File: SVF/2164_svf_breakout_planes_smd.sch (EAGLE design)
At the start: 87 parts, among them IC1 SSM2164S, IC2 TL072, IC3 TL072, IC4 TL072, IC5 TL072, IC6 TL072, U1 THONKICONNNEW, U2 THONKICONNNEW, U3 THONKICONNNEW, U4 THONKICONNNEW, U5 THONKICONNNEW, U6 THONKICONNNEW

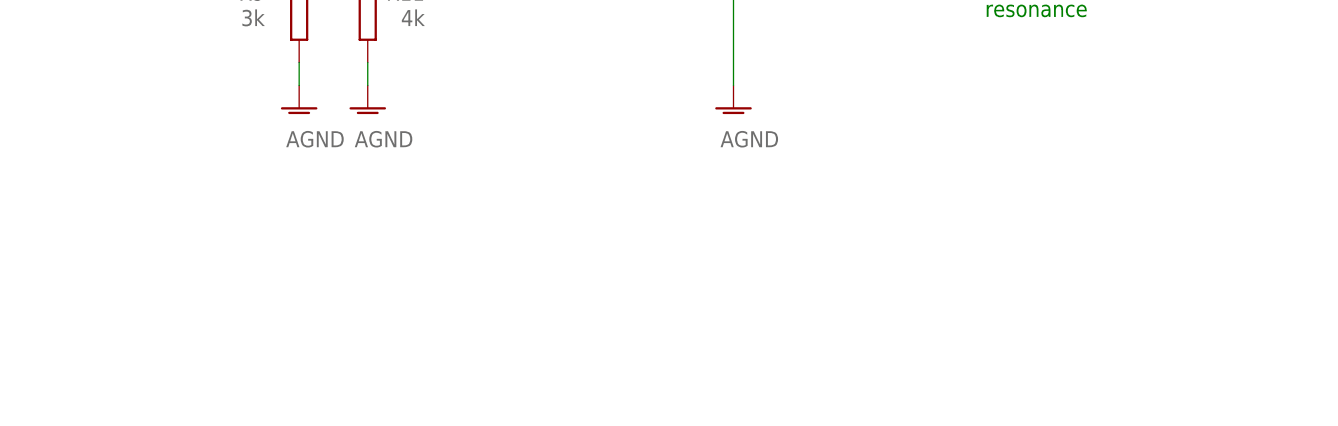
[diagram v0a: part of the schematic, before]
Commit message: Add SMD 0603 version of SVF
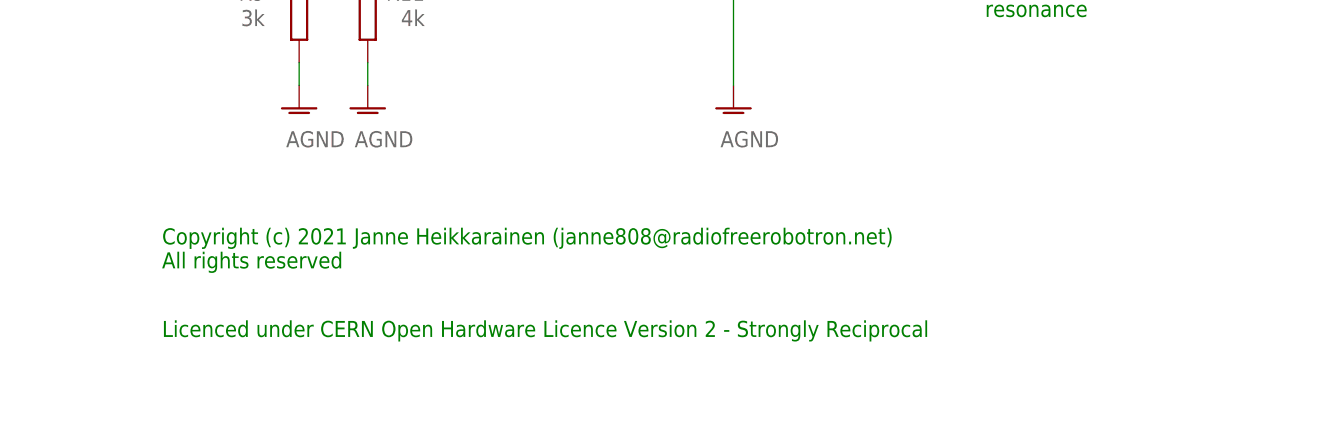
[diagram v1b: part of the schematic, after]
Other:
- note added: "Copyright (c) 2021 Janne Heikkarainen (janne808@radiofreerobotron.net) All rights reserved"
- note added: "Licenced under CERN Open Hardware Licence Version 2 - Strongly Reciprocal"
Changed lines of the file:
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@@
 <grid distance="0.1" unitdist="inch" unit="inch" style="lines" multiple="1" display="no" altdistance="0.01" altunitdist="inch" altunit="inch"/>
 <layers>
-<layer number="1" name="Top" color="4" fill="1" visible="yes" active="no"/>
-<layer number="2" name="Route2" color="16" fill="1" visible="yes" active="no"/>
-<layer number="3" name="Route3" color="17" fill="1" visible="yes" active="no"/>
-<layer number="4" name="Route4" color="18" fill="1" visible="yes" active="no"/>
-<layer number="5" name="Route5" color="19" fill="1" visible="yes" active="no"/>
-<layer number="6" name="Route6" color="25" fill="1" visible="yes" active="no"/>
-<layer number="7" name="Route7" color="26" fill="1" visible="yes" active="no"/>
-<layer number="8" name="Route8" color="27" fill="1" visible="yes" active="no"/>
-<layer number="9" name="Route9" color="28" fill="1" visible="yes" active="no"/>
-<layer number="10" name="Route10" color="29" fill="1" visible="yes" active="no"/>
-<layer number="11" name="Route11" color="30" fill="1" visible="yes" active="no"/>
-<layer number="12" name="Route12" color="20" fill="1" visible="yes" active="no"/>
-<layer number="13" name="Route13" color="21" fill="1" visible="yes" active="no"/>
-<layer number="14" name="Route14" color="22" fill="1" visible="yes" active="no"/>
-<layer number="15" name="Route15" color="23" fill="1" visible="yes" active="no"/>
-<layer number="16" name="Bottom" color="1" fill="1" visible="yes" active="no"/>
-<layer number="17" name="Pads" color="2" fill="1" visible="yes" active="no"/>
-<layer number="18" name="Vias" color="2" fill="1" visible="yes" active="no"/>
-<layer number="19" name="Unrouted" color="6" fill="1" visible="yes" active="no"/>
-<layer number="20" name="Dimension" color="24" fill="1" visible="yes" active="no"/>
-<layer number="21" name="tPlace" color="7" fill="1" visible="yes" active="no"/>
-<layer number="22" name="bPlace" color="7" fill="1" visible="yes" active="no"/>
-<layer number="23" name="tOrigins" color="15" fill="1" visible="yes" active="no"/>
-<layer number="24" name="bOrigins" color="15" fill="1" visible="yes" active="no"/>
-<layer number="25" name="tNames" color="7" fill="1" visible="yes" active="no"/>
-<layer number="26" name="bNames" color="7" fill="1" visible="yes" active="no"/>
-<layer number="27" name="tValues" color="7" fill="1" visible="yes" active="no"/>
-<layer number="28" name="bValues" color="7" fill="1" visible="yes" active="no"/>
+<layer number="1" name="Top" color="4" fill="1" visible="no" active="no"/>
+<layer number="2" name="Route2" color="16" fill="1" visible="no" active="no"/>
+<layer number="3" name="Route3" color="17" fill="1" visible="no" active="no"/>
+<layer number="4" name="Route4" color="18" fill="1" visible="no" active="no"/>
+<layer number="5" name="Route5" color="19" fill="1" visible="no" active="no"/>
+<layer number="6" name="Route6" color="25" fill="1" visible="no" active="no"/>
+<layer number="7" name="Route7" color="26" fill="1" visible="no" active="no"/>
+<layer number="8" name="Route8" color="27" fill="1" visible="no" active="no"/>
+<layer number="9" name="Route9" color="28" fill="1" visible="no" active="no"/>
+<layer number="10" name="Route10" color="29" fill="1" visible="no" active="no"/>
+<layer number="11" name="Route11" color="30" fill="1" visible="no" active="no"/>
+<layer number="12" name="Route12" color="20" fill="1" visible="no" active="no"/>
+<layer number="13" name="Route13" color="21" fill="1" visible="no" active="no"/>
+<layer number="14" name="Route14" color="22" fill="1" visible="no" active="no"/>
+<layer number="15" name="Route15" color="23" fill="1" visible="no" active="no"/>
+<layer number="16" name="Bottom" color="1" fill="1" visible="no" active="no"/>
+<layer number="17" name="Pads" color="2" fill="1" visible="no" active="no"/>
+<layer number="18" name="Vias" color="2" fill="1" visible="no" active="no"/>
+<layer number="19" name="Unrouted" color="6" fill="1" visible="no" active="no"/>
+<layer number="20" name="Dimension" color="24" fill="1" visible="no" active="no"/>
+<layer number="21" name="tPlace" color="7" fill="1" visible="no" active="no"/>
+<layer number="22" name="bPlace" color="7" fill="1" visible="no" active="no"/>
+<layer number="23" name="tOrigins" color="15" fill="1" visible="no" active="no"/>
+<layer number="24" name="bOrigins" color="15" fill="1" visible="no" active="no"/>
+<layer number="25" name="tNames" color="7" fill="1" visible="no" active="no"/>
+<layer number="26" name="bNames" color="7" fill="1" visible="no" active="no"/>
+<layer number="27" name="tValues" color="7" fill="1" visible="no" active="no"/>
+<layer number="28" name="bValues" color="7" fill="1" visible="no" active="no"/>
 <layer number="29" name="tStop" color="7" fill="3" visible="no" active="no"/>
 <layer number="30" name="bStop" color="7" fill="6" visible="no" active="no"/>
@@
 <layer number="35" name="tGlue" color="7" fill="4" visible="no" active="no"/>
 <layer number="36" name="bGlue" color="7" fill="5" visible="no" active="no"/>
-<layer number="37" name="tTest" color="7" fill="1" visible="yes" active="no"/>
-<layer number="38" name="bTest" color="7" fill="1" visible="yes" active="no"/>
+<layer number="37" name="tTest" color="7" fill="1" visible="no" active="no"/>
+<layer number="38" name="bTest" color="7" fill="1" visible="no" active="no"/>
 <layer number="39" name="tKeepout" color="4" fill="11" visible="no" active="no"/>
 <layer number="40" name="bKeepout" color="1" fill="11" visible="no" active="no"/>
@@
 <layer number="44" name="Drills" color="7" fill="1" visible="no" active="no"/>
 <layer number="45" name="Holes" color="7" fill="1" visible="no" active="no"/>
-<layer number="46" name="Milling" color="3" fill="1" visible="yes" active="no"/>
-<layer number="47" name="Measures" color="7" fill="1" visible="yes" active="no"/>
-<layer number="48" name="Document" color="7" fill="1" visible="yes" active="no"/>
-<layer number="49" name="Reference" color="7" fill="1" visible="yes" active="no"/>
-<layer number="50" name="dxf" color="7" fill="1" visible="yes" active="no"/>
-<layer number="51" name="tDocu" color="7" fill="1" visible="yes" active="no"/>
-<layer number="52" name="bDocu" color="7" fill="1" visible="yes" active="no"/>
-<layer number="53" name="tGND_GNDA" color="7" fill="9" visible="yes" active="no"/>
-<layer number="54" name="bGND_GNDA" color="1" fill="9" visible="yes" active="no"/>
-<layer number="56" name="wert" color="7" fill="1" visible="yes" active="no"/>
-<layer number="57" name="tCAD" color="7" fill="1" visible="yes" active="no"/>
-<layer number="59" name="tCarbon" color="7" fill="1" visible="yes" active="no"/>
-<layer number="60" name="bCarbon" color="7" fill="1" visible="yes" active="no"/>
+<layer number="46" name="Milling" color="3" fill="1" visible="no" active="no"/>
+<layer number="47" name="Measures" color="7" fill="1" visible="no" active="no"/>
+<layer number="48" name="Document" color="7" fill="1" visible="no" active="no"/>
+<layer number="49" name="Reference" color="7" fill="1" visible="no" active="no"/>
+<layer number="50" name="dxf" color="7" fill="1" visible="no" active="no"/>
+<layer number="51" name="tDocu" color="7" fill="1" visible="no" active="no"/>
+<layer number="52" name="bDocu" color="7" fill="1" visible="no" active="no"/>
+<layer number="53" name="tGND_GNDA" color="7" fill="9" visible="no" active="no"/>
+<layer number="54" name="bGND_GNDA" color="1" fill="9" visible="no" active="no"/>
+<layer number="56" name="wert" color="7" fill="1" visible="no" active="no"/>
+<layer number="57" name="tCAD" color="7" fill="1" visible="no" active="no"/>
+<layer number="59" name="tCarbon" color="7" fill="1" visible="no" active="no"/>
+<layer number="60" name="bCarbon" color="7" fill="1" visible="no" active="no"/>
 <layer number="88" name="SimResults" color="9" fill="1" visible="yes" active="yes"/>
 <layer number="89" name="SimProbes" color="9" fill="1" visible="yes" active="yes"/>
@@
 <text x="40.64" y="132.08" size="1.778" layer="91">cv1</text>
 <text x="40.64" y="236.22" size="1.778" layer="91">cv2</text>
+<text x="154.94" y="22.86" size="1.778" layer="91">Copyright (c) 2021 Janne Heikkarainen (janne808@radiofreerobotron.net)
+All rights reserved</text>
+<text x="154.94" y="15.24" size="1.778" layer="91">Licenced under CERN Open Hardware Licence Version 2 - Strongly Reciprocal</text>
 </plain>
 <instances>
@@
 </drawing>
 <compatibility>
+<note version="6.3" minversion="6.2.2" severity="warning">
+Since Version 6.2.2 text objects can contain more than one line,
+which will not be processed correctly with this version.
+</note>
 <note version="8.2" severity="warning">
 Since Version 8.2, EAGLE supports online libraries. The ids

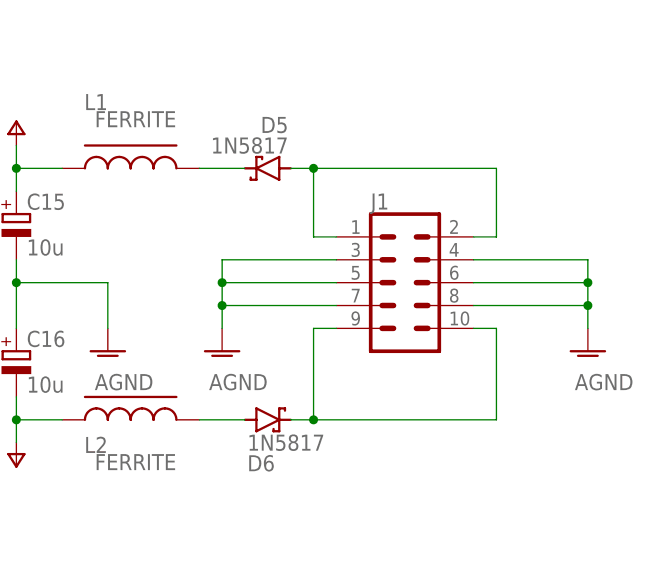
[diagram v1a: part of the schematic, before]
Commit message: Fix backwards footprint graphics for headers and power connector -- note that physical pinouts are unaffected
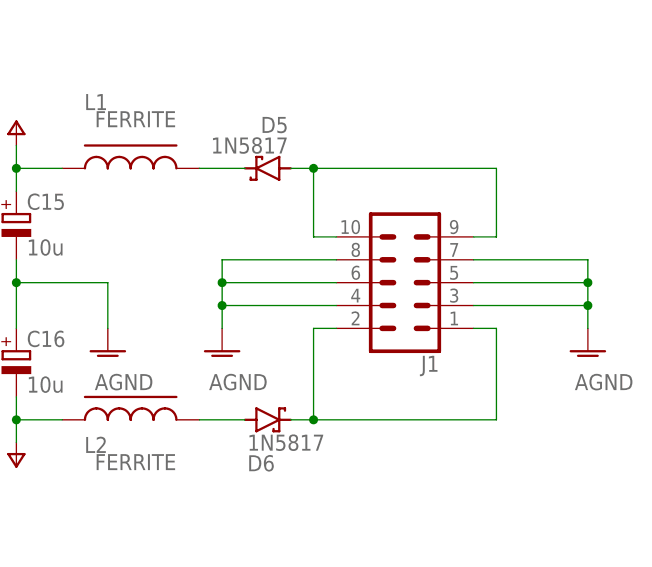
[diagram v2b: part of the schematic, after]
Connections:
- net N$42: now also J1.1, J1.2; no longer J1.10, J1.9
- net N$43: now also J1.10, J1.9; no longer J1.1, J1.2
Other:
- moved on the sheet: J1
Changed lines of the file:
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@@
 <attribute name="VALUE" x="134.62" y="218.44" size="1.778" layer="96" rot="R180"/>
 </instance>
-<instance part="J1" gate="G$1" x="347.98" y="215.9" smashed="yes">
-<attribute name="VALUE" x="344.17" y="205.994" size="1.778" layer="96" font="vector"/>
-<attribute name="NAME" x="344.17" y="224.028" size="1.778" layer="95" font="vector"/>
+<instance part="J1" gate="G$1" x="347.98" y="215.9" smashed="yes" rot="R180">
+<attribute name="VALUE" x="351.79" y="225.806" size="1.778" layer="96" font="vector" rot="R180"/>
+<attribute name="NAME" x="351.79" y="207.772" size="1.778" layer="95" font="vector" rot="R180"/>
 </instance>
 <instance part="AGND25" gate="VR1" x="368.3" y="208.28" smashed="yes">
@@
 <pinref part="AGND25" gate="VR1" pin="AGND"/>
 <wire x1="368.3" y1="210.82" x2="368.3" y2="213.36" width="0.1524" layer="91"/>
-<pinref part="J1" gate="G$1" pin="4"/>
+<pinref part="J1" gate="G$1" pin="7"/>
 <wire x1="368.3" y1="213.36" x2="368.3" y2="215.9" width="0.1524" layer="91"/>
 <wire x1="368.3" y1="215.9" x2="368.3" y2="218.44" width="0.1524" layer="91"/>
-<wire x1="368.3" y1="218.44" x2="355.6" y2="218.44" width="0.1524" layer="91"/>
-<pinref part="J1" gate="G$1" pin="6"/>
+<wire x1="355.6" y1="218.44" x2="368.3" y2="218.44" width="0.1524" layer="91"/>
+<pinref part="J1" gate="G$1" pin="5"/>
 <wire x1="355.6" y1="215.9" x2="368.3" y2="215.9" width="0.1524" layer="91"/>
 <junction x="368.3" y="215.9"/>
-<pinref part="J1" gate="G$1" pin="8"/>
+<pinref part="J1" gate="G$1" pin="3"/>
 <wire x1="355.6" y1="213.36" x2="368.3" y2="213.36" width="0.1524" layer="91"/>
 <junction x="368.3" y="213.36"/>
@@
 <pinref part="AGND26" gate="VR1" pin="AGND"/>
 <wire x1="327.66" y1="210.82" x2="327.66" y2="213.36" width="0.1524" layer="91"/>
-<pinref part="J1" gate="G$1" pin="3"/>
+<pinref part="J1" gate="G$1" pin="8"/>
 <wire x1="327.66" y1="213.36" x2="327.66" y2="215.9" width="0.1524" layer="91"/>
 <wire x1="327.66" y1="215.9" x2="327.66" y2="218.44" width="0.1524" layer="91"/>
-<wire x1="327.66" y1="218.44" x2="340.36" y2="218.44" width="0.1524" layer="91"/>
-<pinref part="J1" gate="G$1" pin="5"/>
+<wire x1="340.36" y1="218.44" x2="327.66" y2="218.44" width="0.1524" layer="91"/>
+<pinref part="J1" gate="G$1" pin="6"/>
 <wire x1="340.36" y1="215.9" x2="327.66" y2="215.9" width="0.1524" layer="91"/>
 <junction x="327.66" y="215.9"/>
-<pinref part="J1" gate="G$1" pin="7"/>
+<pinref part="J1" gate="G$1" pin="4"/>
 <wire x1="340.36" y1="213.36" x2="327.66" y2="213.36" width="0.1524" layer="91"/>
 <junction x="327.66" y="213.36"/>
@@
 <net name="N$42" class="0">
 <segment>
-<pinref part="J1" gate="G$1" pin="9"/>
-<wire x1="340.36" y1="210.82" x2="337.82" y2="210.82" width="0.1524" layer="91"/>
 <pinref part="D6" gate="G$1" pin="C"/>
 <wire x1="335.28" y1="200.66" x2="337.82" y2="200.66" width="0.1524" layer="91"/>
@@
 <wire x1="337.82" y1="200.66" x2="358.14" y2="200.66" width="0.1524" layer="91"/>
 <junction x="337.82" y="200.66"/>
-<pinref part="J1" gate="G$1" pin="10"/>
-<wire x1="358.14" y1="210.82" x2="355.6" y2="210.82" width="0.1524" layer="91"/>
 <wire x1="358.14" y1="200.66" x2="358.14" y2="210.82" width="0.1524" layer="91"/>
+<pinref part="J1" gate="G$1" pin="2"/>
+<wire x1="340.36" y1="210.82" x2="337.82" y2="210.82" width="0.1524" layer="91"/>
+<pinref part="J1" gate="G$1" pin="1"/>
+<wire x1="355.6" y1="210.82" x2="358.14" y2="210.82" width="0.1524" layer="91"/>
 </segment>
 </net>
 <net name="N$43" class="0">
 <segment>
-<pinref part="J1" gate="G$1" pin="1"/>
-<wire x1="340.36" y1="220.98" x2="337.82" y2="220.98" width="0.1524" layer="91"/>
 <wire x1="337.82" y1="220.98" x2="337.82" y2="228.6" width="0.1524" layer="91"/>
 <pinref part="D5" gate="G$1" pin="A"/>
@@
 <junction x="337.82" y="228.6"/>
 <wire x1="358.14" y1="228.6" x2="358.14" y2="220.98" width="0.1524" layer="91"/>
-<pinref part="J1" gate="G$1" pin="2"/>
-<wire x1="358.14" y1="220.98" x2="355.6" y2="220.98" width="0.1524" layer="91"/>
-</segment>
-</net>
+<pinref part="J1" gate="G$1" pin="9"/>
+<wire x1="355.6" y1="220.98" x2="358.14" y2="220.98" width="0.1524" layer="91"/>
+<pinref part="J1" gate="G$1" pin="10"/>
+<wire x1="340.36" y1="220.98" x2="337.82" y2="220.98" width="0.1524" layer="91"/>
+</segment>
+</net>
